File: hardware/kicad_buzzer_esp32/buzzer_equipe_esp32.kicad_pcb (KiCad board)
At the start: 2 copper layers, 70 x 103 mm, 8 parts, among them J2 Module charge TP4056+protect+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, J3 Module vibreur IN/VCC/GND - C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, SW1 Bouton BUZZ (fils volants) - 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, SW2 Interrupteur marche/arret (fi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, U1L ESP32 colonne gauche (broches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, U1R ESP32 colonne droite (broches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

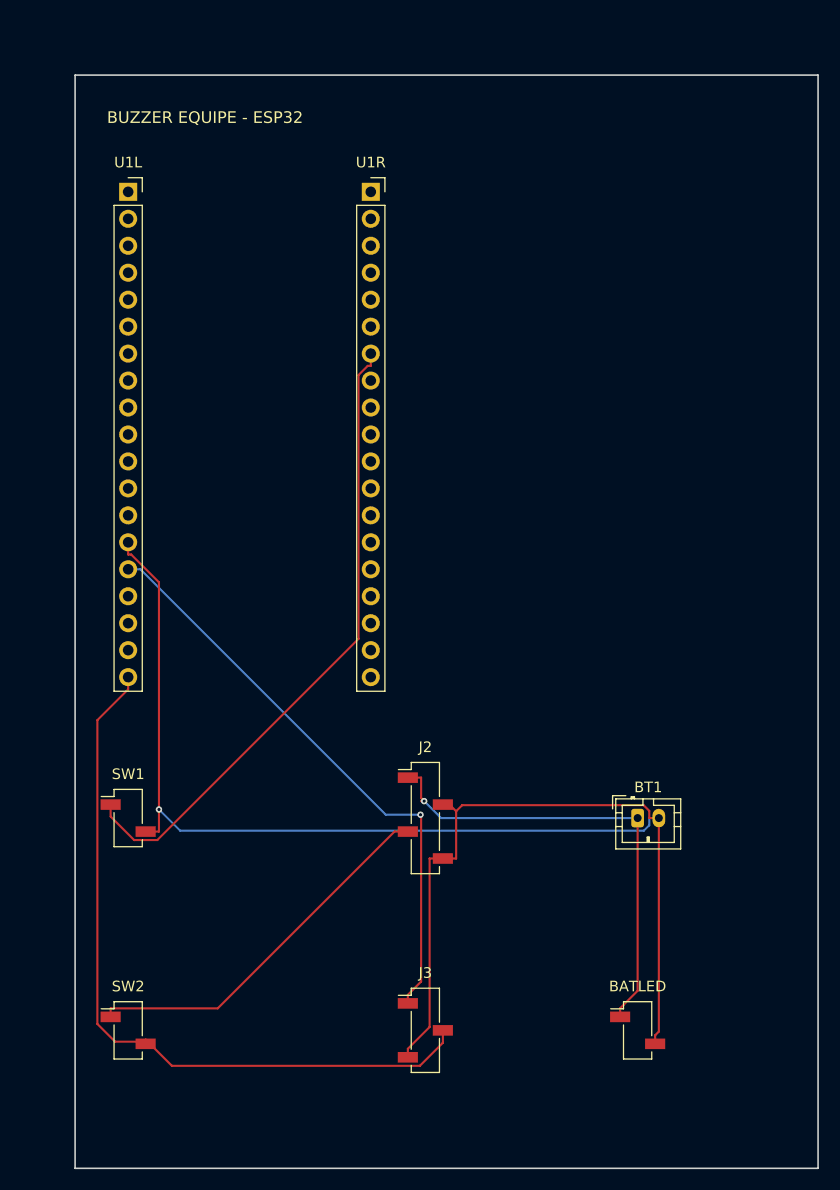
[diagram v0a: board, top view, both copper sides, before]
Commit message: hardware: carte ESP32 equipe 65x50mm, BOM CSV, libelle J_MEGA hub
ESP32 equipe reduite a 65x50mm (U1L/U1R et J2/J3 pivotes a 90 degres),
reroutee, DRC sans clearance ni connexion manquante. Gerbers regeneres.
Fichiers BOM CSV ajoutes pour les 3 cartes. Hub : libelle J_MEGA
TX1/RX1 (pins 18/19) au lieu de TX3/RX3, sans changement de routage.

Co-Authored-By: Claude Sonnet 5 <noreply@anthropic.com>
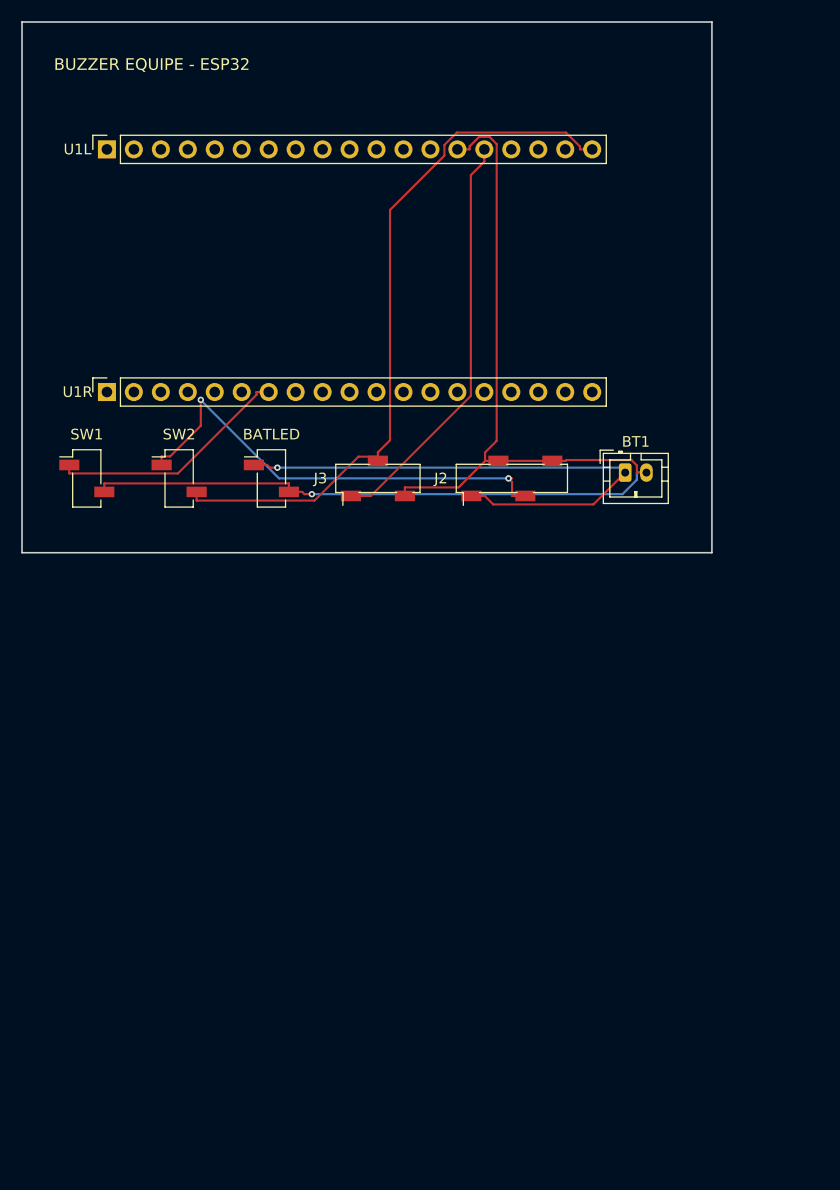
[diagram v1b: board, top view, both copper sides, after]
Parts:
- moved BATLED 62.4 mm to (23.5, 43.0)
- moved SW2 52.2 mm to (14.8, 43.0)
- moved J3 52.2 mm to (33.5, 43.0), turned to 90 degrees
- moved J2 33.0 mm to (46.1, 43.0), turned to 90 degrees
- moved BT1 32.6 mm to (56.8, 42.5)
- moved SW1 32.2 mm to (6.10, 43.0)
- moved U1R 31.2 mm to (8.00, 34.9), turned to 90 degrees
- moved U1L 4.47 mm to (8.00, 12.0), turned to 90 degrees
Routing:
- net BTN_SIG: track 60.8 -> 22.9 mm
- net GND: track 148.4 -> 114.5 mm
- net VIBE_IN: track 55.4 -> 39.0 mm, vias 1 -> 0
- net VCC_5V_RAW: track 35.7 -> 43.9 mm, vias 0 -> 2
- net BAT_PLUS: track 44.3 -> 51.3 mm
- net VCC_5V_SW: track 70.6 -> 67.2 mm
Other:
- board size 70 x 103 mm -> 65 x 50 mm
